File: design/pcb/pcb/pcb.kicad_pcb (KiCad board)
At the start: 2 copper layers, 68.5 x 201.8 mm, 0 parts

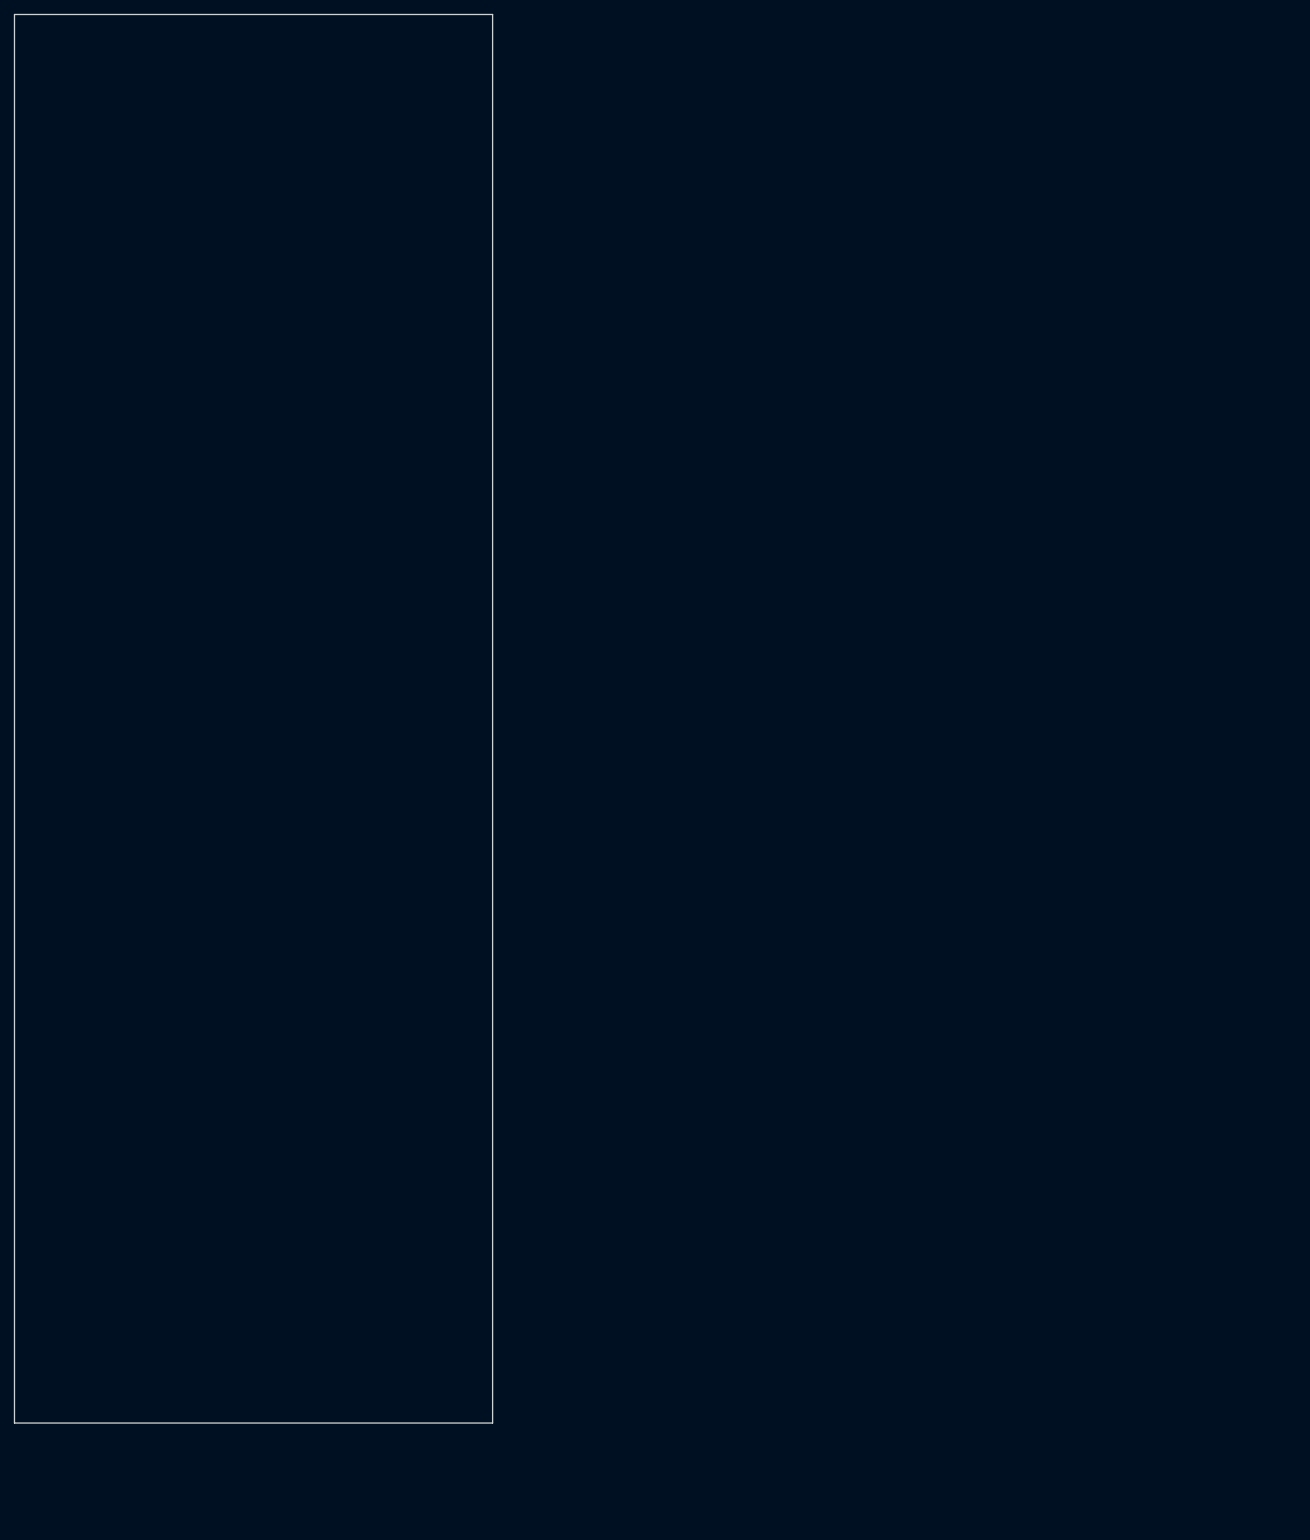
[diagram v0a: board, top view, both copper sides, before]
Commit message: Trying to route PCB. May require changing how footprints are generated.
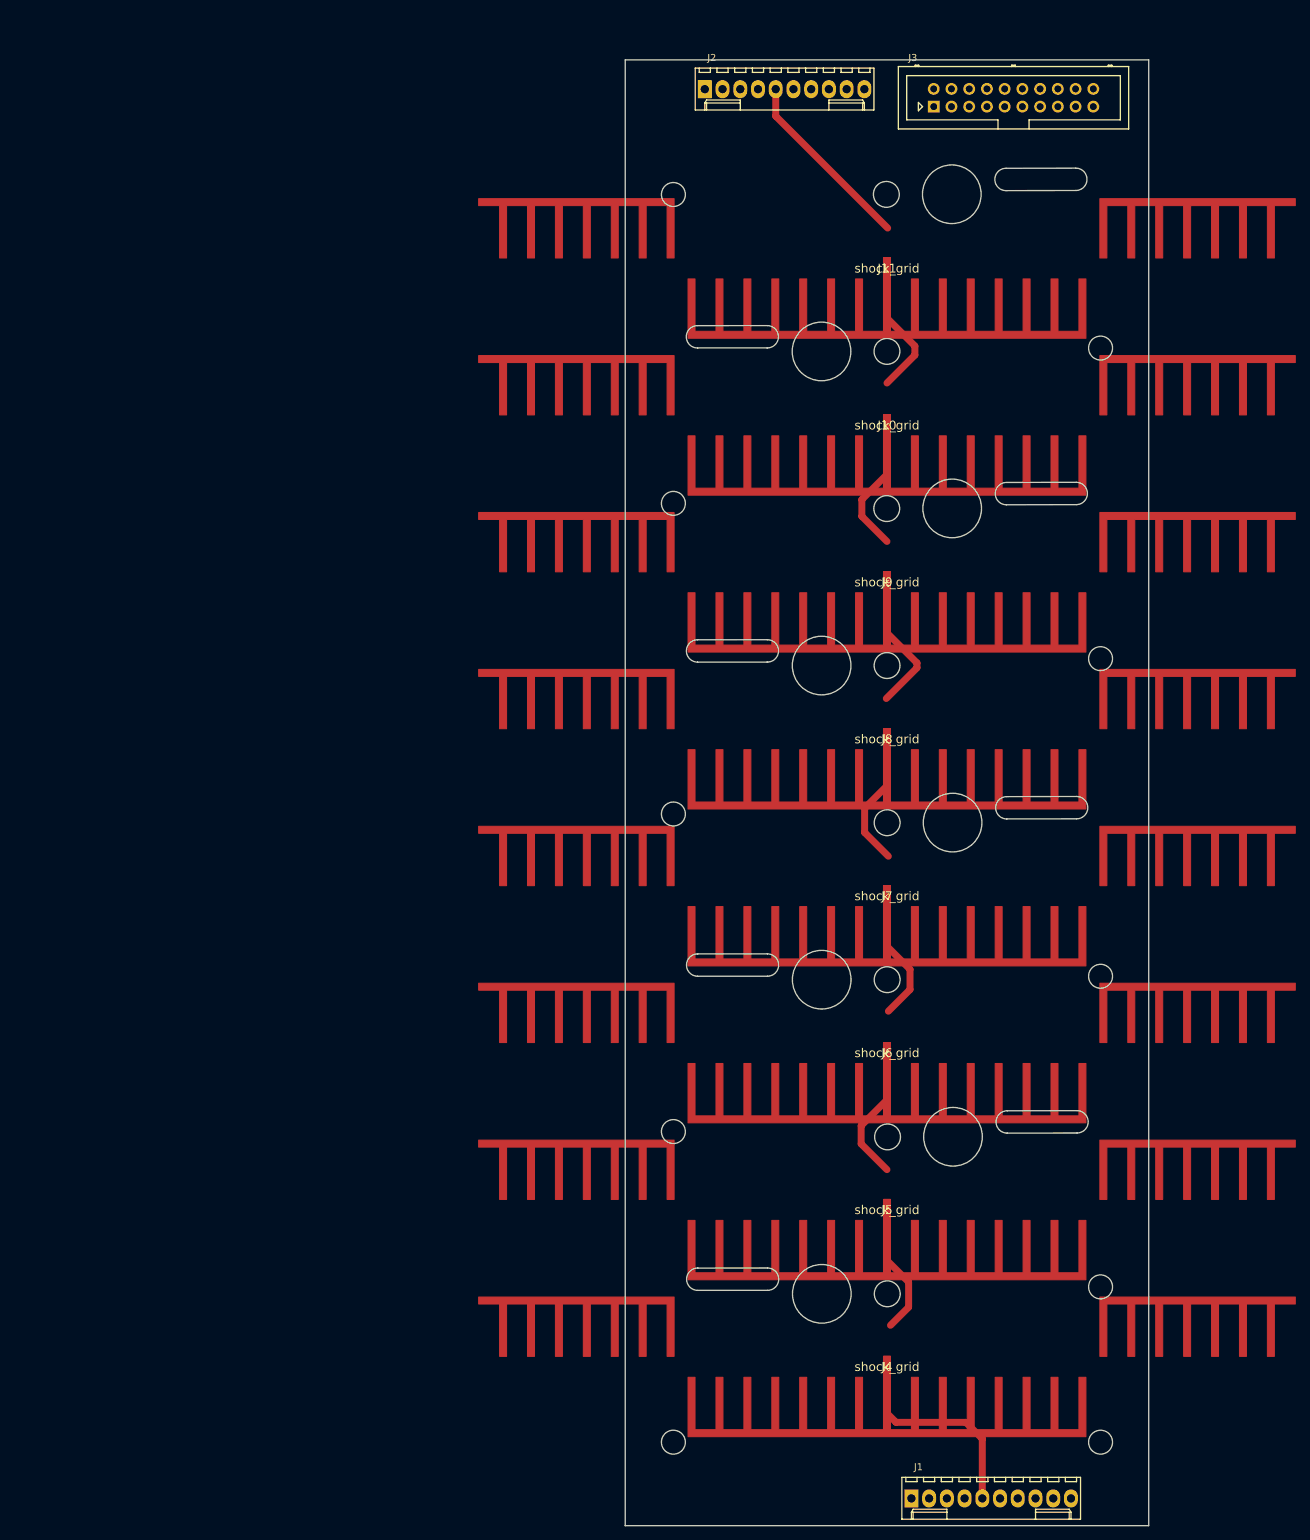
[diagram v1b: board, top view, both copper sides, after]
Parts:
- added J1: Conn_01x10_Male, Connectors_Molex:Molex_KK-6410-10_10x2.54mm_Straight, F.Cu at (128.5, 212.6)
- added J10: shock_grid, footprints:electrode, F.Cu at (125.0, 58.9)
- added J11: shock_grid, footprints:electrode, F.Cu at (125.0, 36.4)
- added J2: Conn_01x10_Male, Connectors_Molex:Molex_KK-6410-10_10x2.54mm_Straight, F.Cu at (98.9, 10.7)
- added J3: Conn_02x10_Top_Bottom, Connectors_Multicomp:Multicomp_MC9A12-2034_2x10x2.54mm_Straight, F.Cu at (131.7, 13.2)
- added J4: shock_grid, footprints:electrode, F.Cu at (125.0, 193.8)
- added J5: shock_grid, footprints:electrode, F.Cu at (125.0, 171.3)
- added J6: shock_grid, footprints:electrode, F.Cu at (125.0, 148.8)
- added J7: shock_grid, footprints:electrode, F.Cu at (125.0, 126.3)
- added J8: shock_grid, footprints:electrode, F.Cu at (125.0, 103.8)
- added J9: shock_grid, footprints:electrode, F.Cu at (125.0, 81.3)
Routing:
- net Net-(J1-Pad5): track 0.00 -> 193.8 mm
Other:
- board size 68.5 x 201.8 mm -> 75 x 210 mm

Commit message: Made two custom (S/D)IP footprints with slightly larger clearances. Mostly fixed custom electrode footprint pad anchor points.
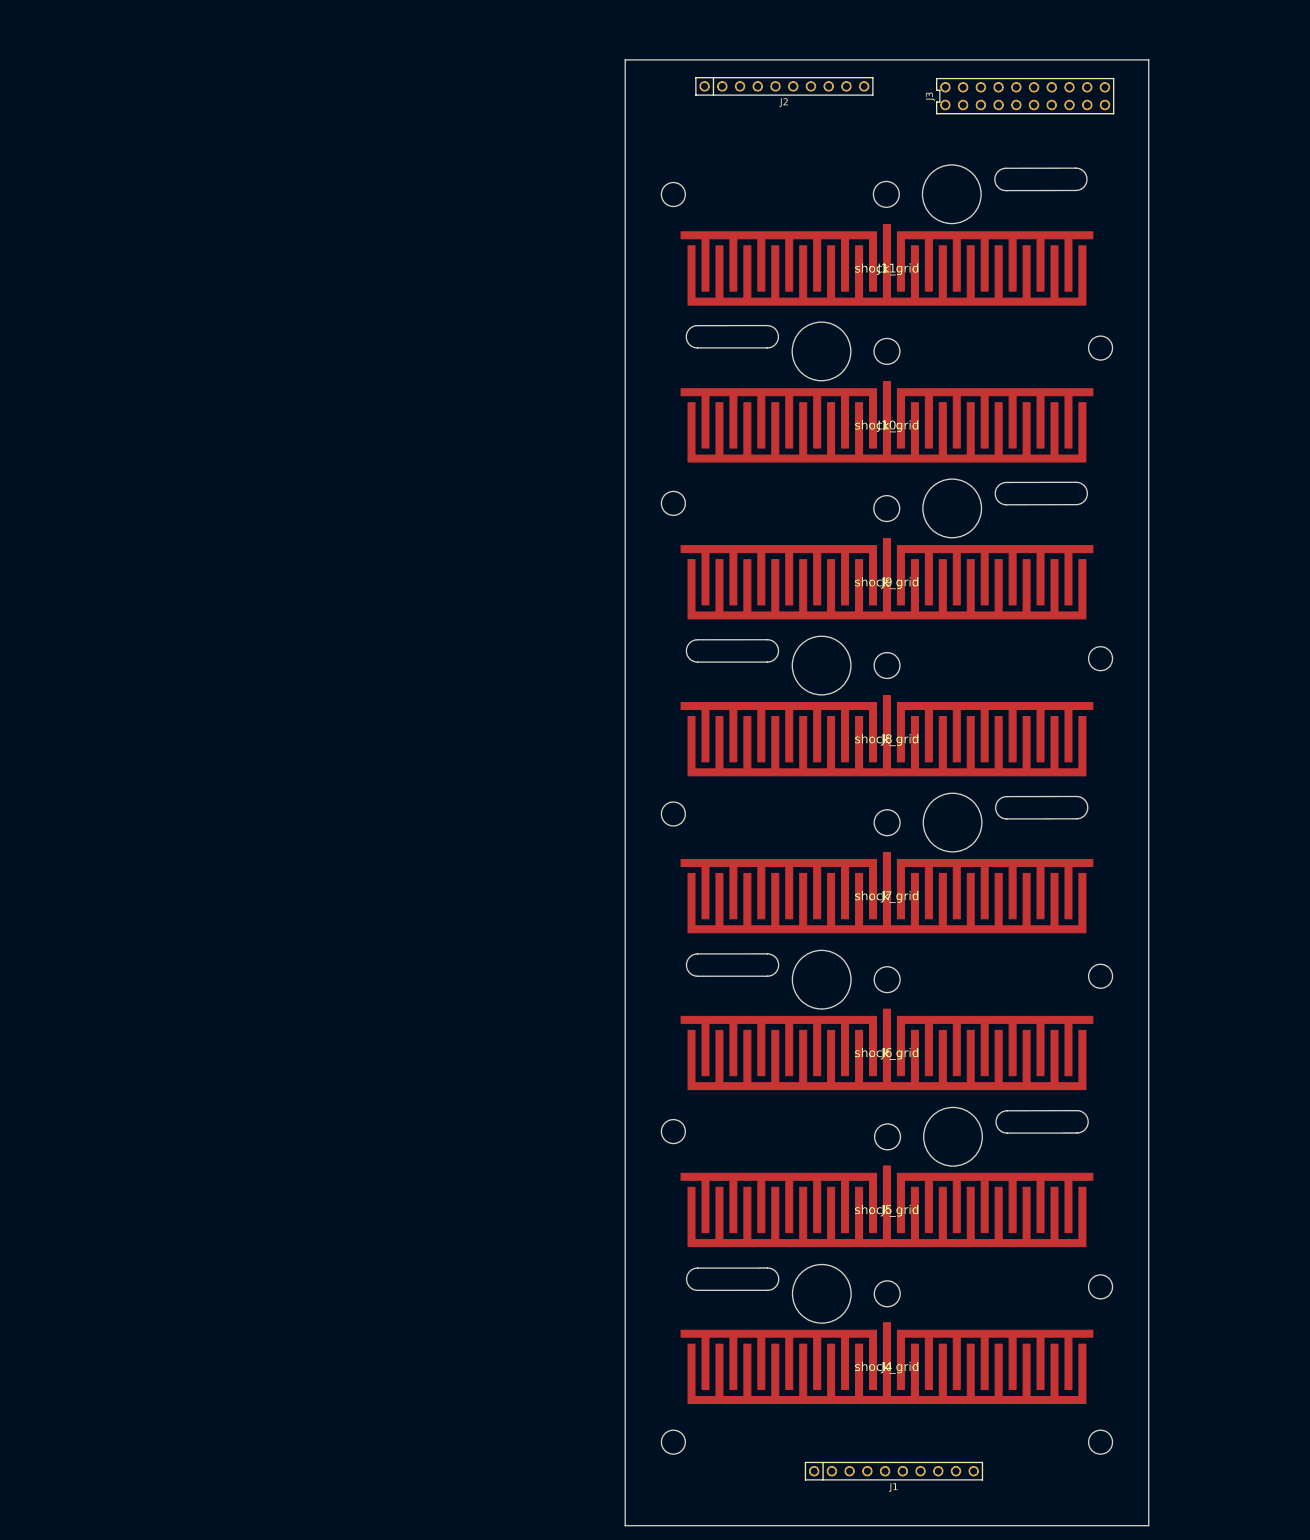
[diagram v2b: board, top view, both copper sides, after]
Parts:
- J1, J2: footprint Connectors_Molex:Molex_KK-6410-10_10x2.54mm_Straight -> footprints:SIP-10_2.54mm_1mm_clearance
- J3: footprint Connectors_Multicomp:Multicomp_MC9A12-2034_2x10x2.54mm_Straight -> footprints:DIP-2x10_2.54mm_1mm_clearance
- moved J3 13.2 mm to (144.8, 11.7)
- moved J2 11.4 mm to (110.3, 10.3)
- moved J1 4.63 mm to (126.0, 208.7)
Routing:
- net Net-(J1-Pad5): track 193.8 -> 0.00 mm
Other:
- net class Default: clearance 0.2 -> 0.6
- rule trace_clearance: 0.2 -> 0.6

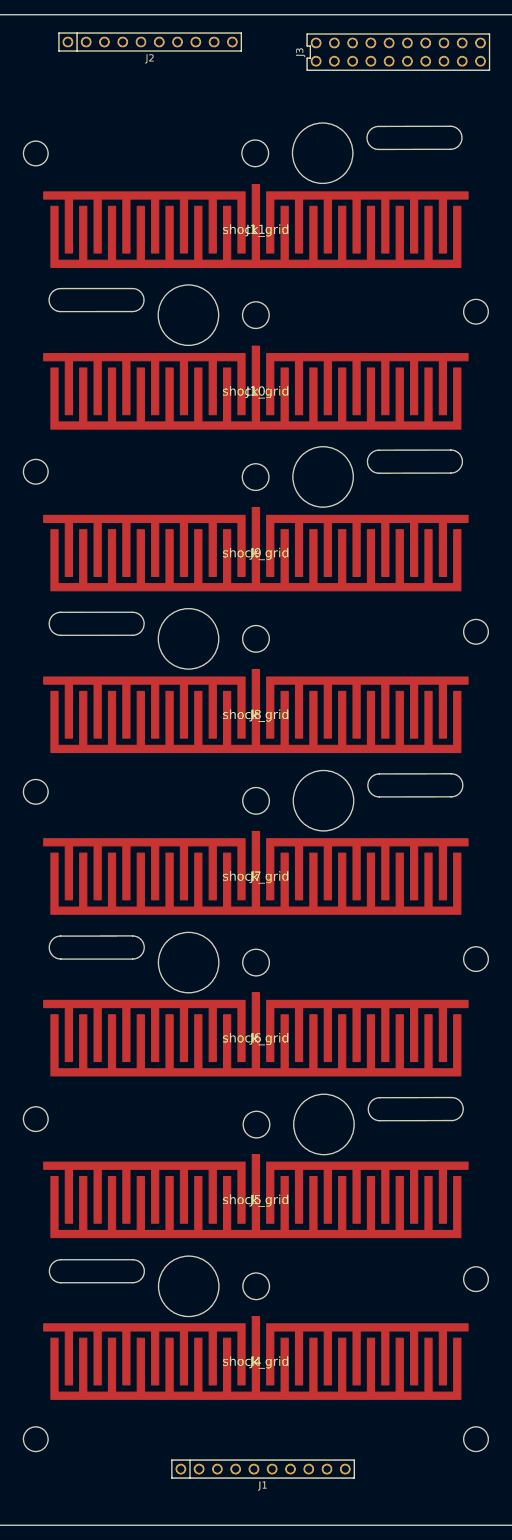
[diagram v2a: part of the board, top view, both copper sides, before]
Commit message: Changed layer set in electrode_vertices + layer references are on. Placing pair of connectors symmetrically in make_board and setting title block there.
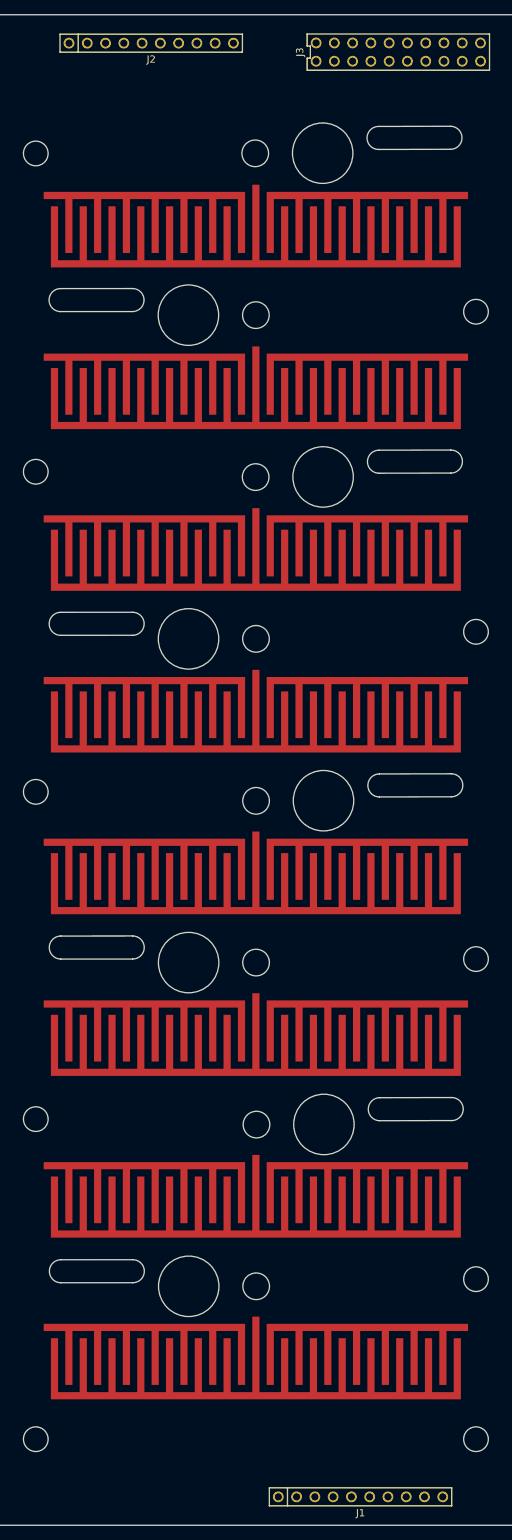
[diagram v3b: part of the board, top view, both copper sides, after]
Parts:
- moved J1 14.1 mm to (139.6, 212.6)
- moved J2 0.22 mm to (110.4, 10.5)

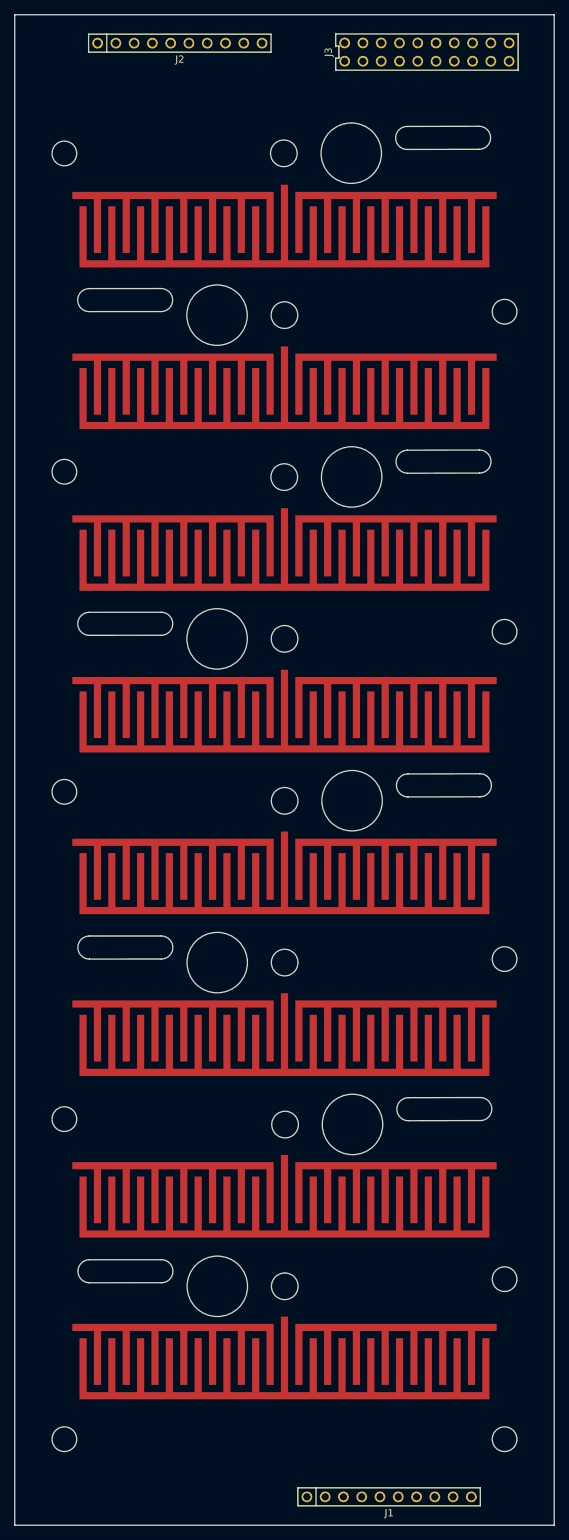
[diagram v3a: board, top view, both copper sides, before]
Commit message: Re-ordered some pins in sch and regenerated netlist. Increased y margin to connectors for extra space for routing. Finished routing of board with original footprint geometry.
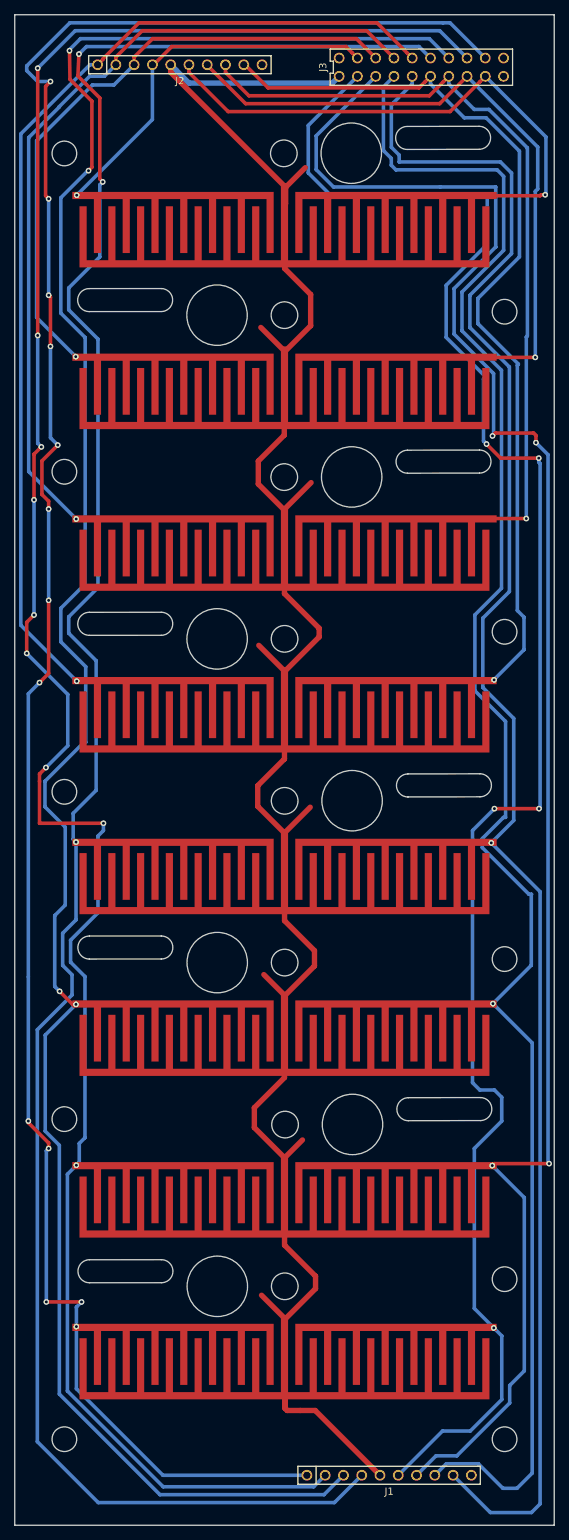
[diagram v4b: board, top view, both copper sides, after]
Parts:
- moved J1 3.00 mm to (139.6, 209.6)
- moved J2 3.00 mm to (110.4, 13.5)
- moved J3 2.24 mm to (144.0, 13.8)
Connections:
- J2 pad 6: Net-(J2-Pad6) -> Net-(J11-Pad1)
- J2 pad 7: Net-(J2-Pad7) -> Net-(J10-Pad1)
- J2 pad 8: Net-(J10-Pad1) -> Net-(J2-Pad8)
- J2 pad 9: Net-(J11-Pad1) -> Net-(J2-Pad9)
- J3 pad 6: Net-(J2-Pad6) -> Net-(J2-Pad9)
- J3 pad 7: Net-(J2-Pad7) -> Net-(J2-Pad8)
- J8 pad 1: Net-(J2-Pad6) -> Net-(J2-Pad9)
- J9 pad 1: Net-(J2-Pad7) -> Net-(J2-Pad8)
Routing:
- net Net-(J1-Pad2): track 0.00 -> 307.0 mm, vias 0 -> 9
- net Net-(J1-Pad4): track 0.00 -> 306.3 mm, vias 0 -> 3
- net Net-(J1-Pad3): track 0.00 -> 303.6 mm, vias 0 -> 4
- net Net-(J1-Pad1): track 0.00 -> 301.6 mm, vias 0 -> 13
- net Net-(J1-Pad5): track 0.00 -> 297.5 mm
- net Net-(J1-Pad6): track 0.00 -> 253.3 mm, vias 0 -> 5
- net Net-(J1-Pad7): track 0.00 -> 250.9 mm, vias 0 -> 4
- net Net-(J1-Pad8): track 0.00 -> 243.5 mm, vias 0 -> 1
- net Net-(J1-Pad9): track 0.00 -> 241.7 mm, vias 0 -> 1
- net Net-(J2-Pad1): track 0.00 -> 142.2 mm, vias 0 -> 1
- net Net-(J2-Pad9): track 0.00 -> 125.7 mm, vias 0 -> 1
- net Net-(J2-Pad2): track 0.00 -> 114.9 mm, vias 0 -> 1
- net Net-(J2-Pad8): track 0.00 -> 106.7 mm, vias 0 -> 1
- net Net-(J10-Pad1): track 0.00 -> 89.1 mm, vias 0 -> 1
- net Net-(J10-Pad2): track 0.00 -> 87.0 mm, vias 0 -> 1
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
